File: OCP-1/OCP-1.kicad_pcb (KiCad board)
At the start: 2 copper layers, 15 parts, among them X1 Клеммник_х2

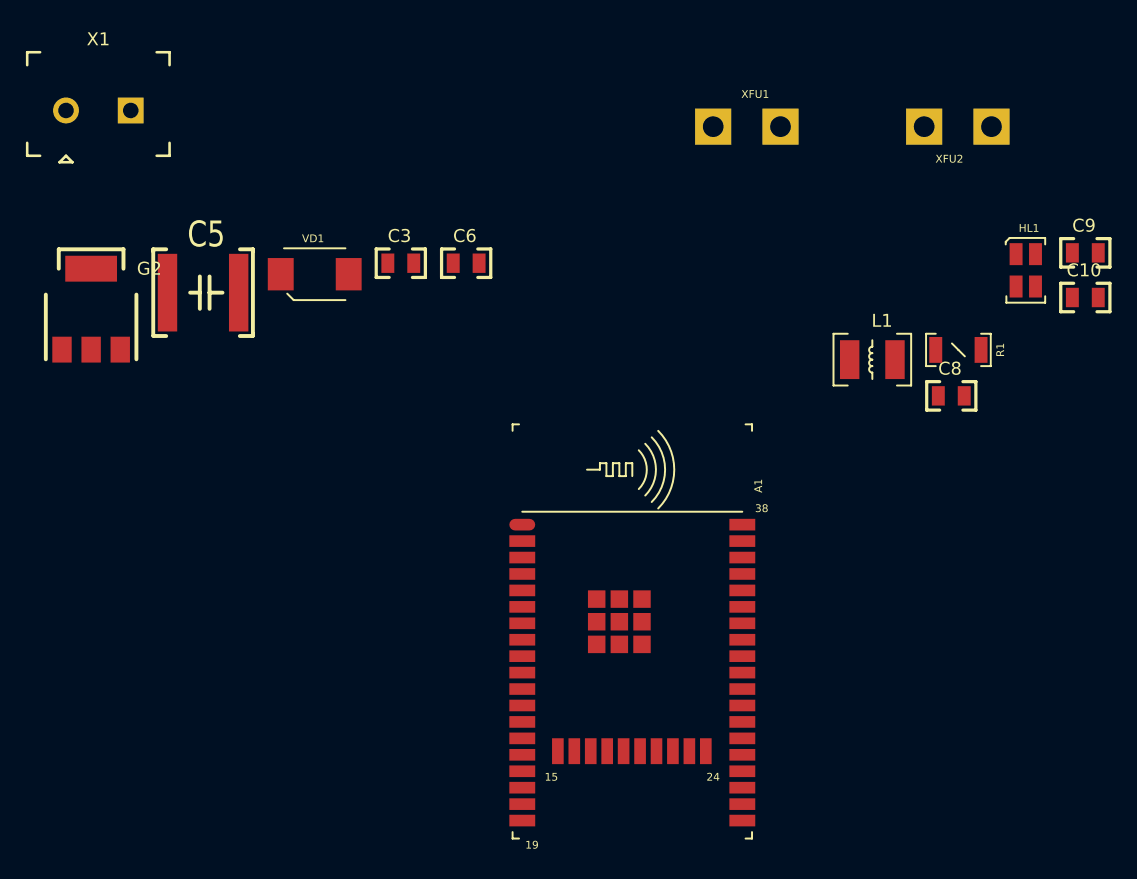
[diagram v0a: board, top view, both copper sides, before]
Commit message: теперь это альтиметр со звуковым оповещением
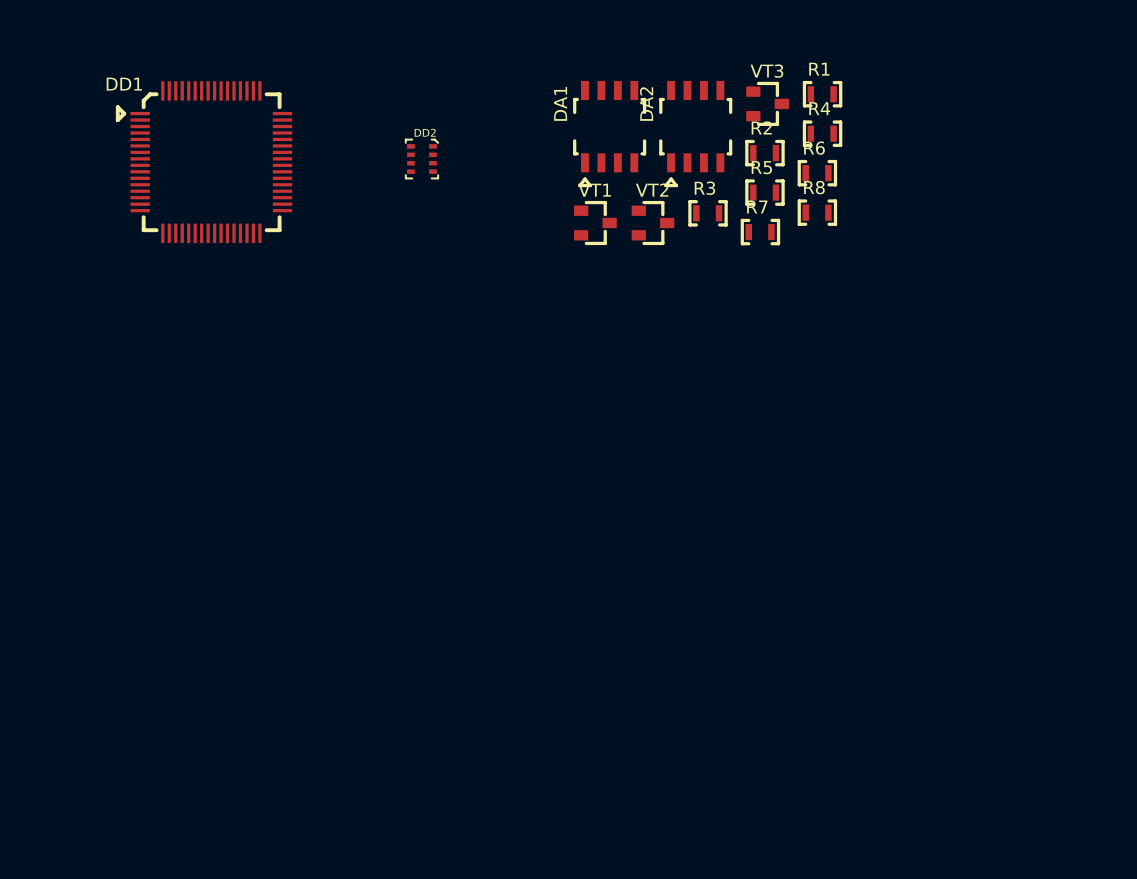
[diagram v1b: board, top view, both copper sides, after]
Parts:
- removed A1: модуль_esp32_wrover_OR_wroom32_SMD, N_A:ESP32_WROVER_or_WROOM32_pnp
- removed C10, C3, C6, C8, C9: Конденсатор_керамический, N_RLC:Конденсатор_SMD_0805
- removed C5: Конденсатор_керамический, N_RLC:Конденсатор_SMD_2220
- removed G2: стабилизатор_нерегулируемый_LM1117S33, N_VD_HL:Транзистор_NPN_SOT223
- removed HL1: Светодиод_сдвоенный_KPB-3025SURKCGKC, N_VD_HL:Светодиод_SMD_m3025
- removed L1: Чип-индуктивность, N_RLC:Чип-индуктивность_SMD_1210
- removed VD1: Диод_шоттки_SK16, N_VD_HL:Диод_SMB_pnp
- removed X1: Клеммник_х2, N_X:Клеммник_х2_шаг5
- removed XFU1, XFU2: Держатель_предохранителя_KLS5-266, N_X:Держатель_5х20
- added DA1: ОУ_LMx58, N_DD:SO-8, F.Cu at (167.0, 67.5)
- added DA2: ОУ_LMx58, N_DD:SO-8, F.Cu at (173.7, 67.5)
- added DD1: 1986ВЕ92QL, N_DD:Микросхема_1986ВЕ92QL, F.Cu at (125.0, 62.5)
- added DD2: BMP280, N_DD:BMP280, F.Cu at (152.5, 70.0)
- added R2: Резистор_0,065Вт, N_RLC:Резистор_SMD_0603_0,065_Вт, F.Cu at (179.0, 69.5)
- added R3: Резистор_0,065Вт, N_RLC:Резистор_SMD_0603_0,065_Вт, F.Cu at (174.6, 74.2)
- added R4: Резистор_0,065Вт, N_RLC:Резистор_SMD_0603_0,065_Вт, F.Cu at (183.4, 68.0)
- added R5: Резистор_0,065Вт, N_RLC:Резистор_SMD_0603_0,065_Вт, F.Cu at (179.0, 72.6)
- added R6: Резистор_0,065Вт, N_RLC:Резистор_SMD_0603_0,065_Вт, F.Cu at (183.0, 71.1)
- added R7: Резистор_0,065Вт, N_RLC:Резистор_SMD_0603_0,065_Вт, F.Cu at (178.6, 75.6)
- added R8: Резистор_0,065Вт, N_RLC:Резистор_SMD_0603_0,065_Вт, F.Cu at (183.0, 74.1)
- added VT1: Транзистор_полевой_P-канал(IRLML2246TRPBF), N_VD_HL:Транзистор_IRLML6344TR_SOT-23, F.Cu at (165.9, 74.9)
- added VT2: Транзистор_полевой_P-канал(IRLML2246TRPBF), N_VD_HL:Транзистор_IRLML6344TR_SOT-23, F.Cu at (170.3, 74.9)
- added VT3: Транзистор_полевой_N-IRLML6344TR, N_VD_HL:Транзистор_IRLML6344TR_SOT-23, F.Cu at (179.2, 65.7)
- R1: value Резистор_0,25Вт -> Резистор_0,065Вт; footprint N_RLC:Резистор_SMD_1206-0,25_Вт_pnp -> N_RLC:Резистор_SMD_0603_0,065_Вт
- moved R1 22.4 mm to (183.4, 65.0)
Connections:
- R1 pad 2: Net-(G1-Pad1) -> /GND

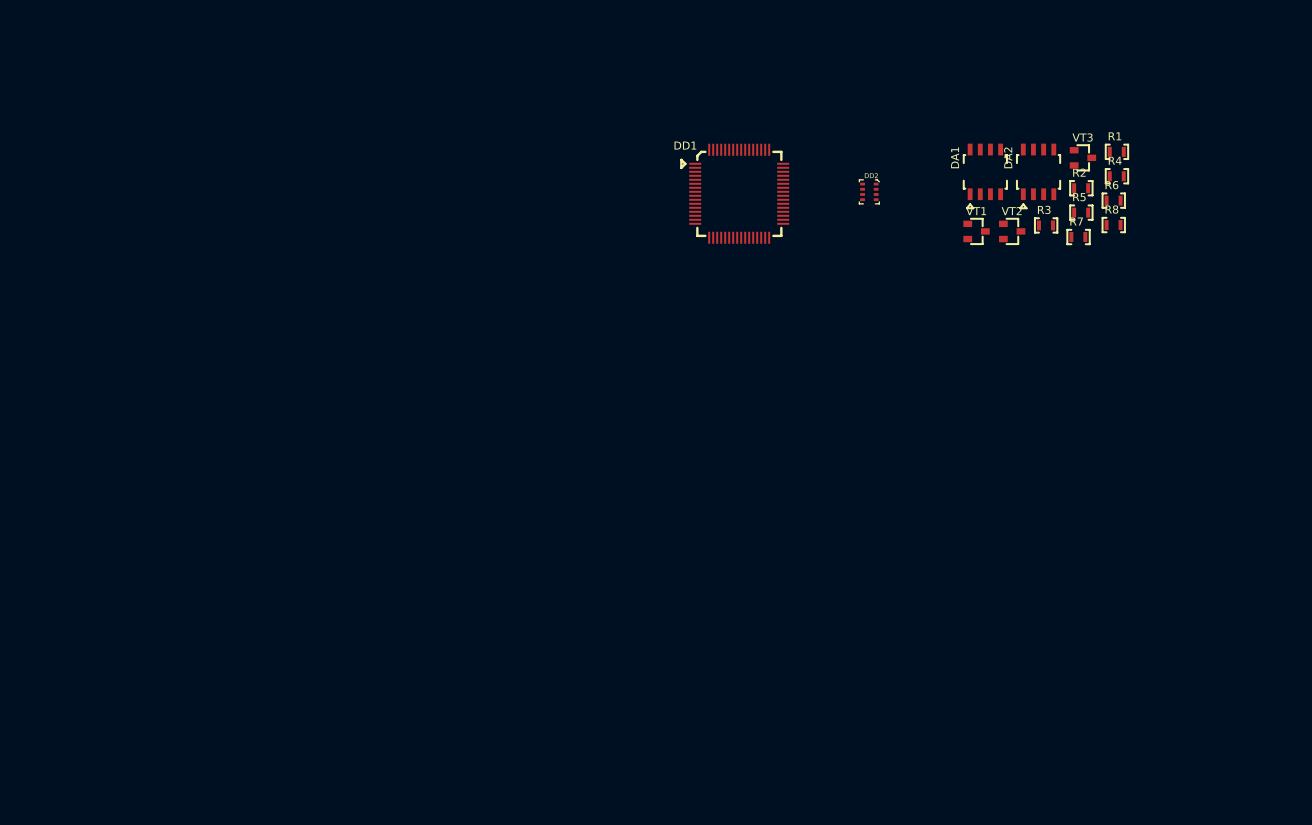
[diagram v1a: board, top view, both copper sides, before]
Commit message: схема заряда аккумулятора и требования к питанию периферии
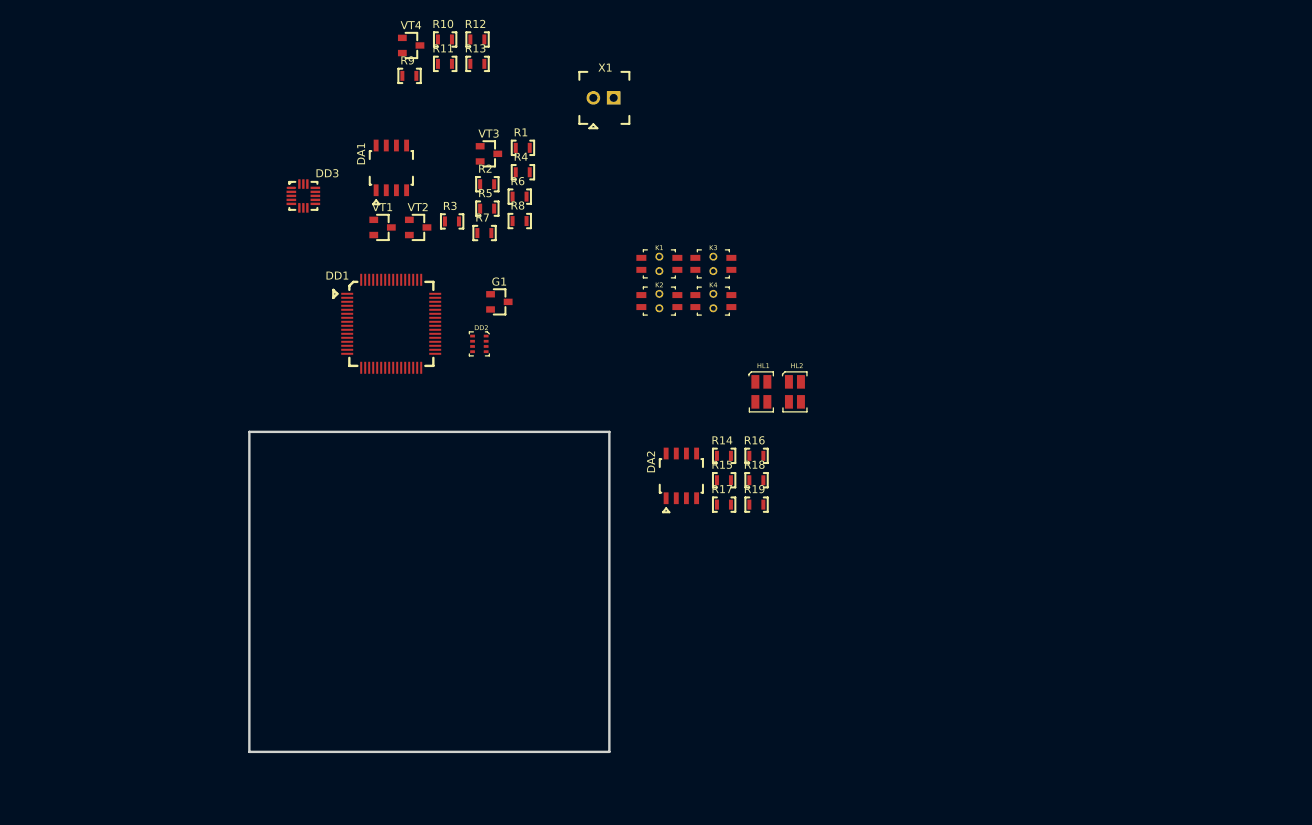
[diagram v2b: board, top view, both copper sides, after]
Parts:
- added DD3: LIS3DH, N_DD:акселерометр_LIS3DH, F.Cu at (81.8, 70.5)
- added G1: ИОП_LM4040BIM3-2.5_NOPB, N_VD_HL:Транзистор_IRLML6344TR_SOT-23, F.Cu at (106.2, 83.8)
- added HL1: Светодиод_сдвоенный_KPB-3025SURKCGKC, N_VD_HL:Светодиод_SMD_m3025, F.Cu at (138.2, 93.8)
- added HL2: Светодиод_сдвоенный_KPB-3025SURKCGKC, N_VD_HL:Светодиод_SMD_m3025, F.Cu at (142.4, 93.8)
- added K1: Кнопка_KLS7-TS5401-1.35-250-T, N_X:Кнопка_KLS7-TS5401, F.Cu at (124.0, 79.8)
- added K2: Кнопка_KLS7-TS5401-1.35-250-T, N_X:Кнопка_KLS7-TS5401, F.Cu at (124.0, 84.4)
- added K3: Кнопка_KLS7-TS5401-1.35-250-T, N_X:Кнопка_KLS7-TS5401, F.Cu at (130.8, 79.8)
- added K4: Кнопка_KLS7-TS5401-1.35-250-T, N_X:Кнопка_KLS7-TS5401, F.Cu at (130.8, 84.4)
- added R10: Резистор_0,065Вт, N_RLC:Резистор_SMD_0603_0,065_Вт, F.Cu at (99.5, 51.0)
- added R11: Резистор_0,065Вт, N_RLC:Резистор_SMD_0603_0,065_Вт, F.Cu at (99.5, 54.0)
- added R12: Резистор_0,065Вт, N_RLC:Резистор_SMD_0603_0,065_Вт, F.Cu at (103.5, 51.0)
- added R13: Резистор_0,065Вт, N_RLC:Резистор_SMD_0603_0,065_Вт, F.Cu at (103.5, 54.0)
- added R14: Резистор_0,065Вт, N_RLC:Резистор_SMD_0603_0,065_Вт, F.Cu at (134.3, 103.0)
- added R15: Резистор_0,065Вт, N_RLC:Резистор_SMD_0603_0,065_Вт, F.Cu at (134.3, 106.0)
- added R16: Резистор_0,065Вт, N_RLC:Резистор_SMD_0603_0,065_Вт, F.Cu at (138.4, 103.0)
- added R17: Резистор_0,065Вт, N_RLC:Резистор_SMD_0603_0,065_Вт, F.Cu at (134.3, 109.1)
- added R18: Резистор_0,065Вт, N_RLC:Резистор_SMD_0603_0,065_Вт, F.Cu at (138.4, 106.0)
- added R19: Резистор_0,065Вт, N_RLC:Резистор_SMD_0603_0,065_Вт, F.Cu at (138.4, 109.1)
- added R9: Резистор_0,065Вт, N_RLC:Резистор_SMD_0603_0,065_Вт, F.Cu at (95.0, 55.5)
- added VT4: Транзистор_полевой_P-канал(IRLML2246TRPBF), N_VD_HL:Транзистор_IRLML6344TR_SOT-23, F.Cu at (95.2, 51.7)
- added X1: Клеммник_х2, N_X:Клеммник_х2_шаг2.54, F.Cu at (118.0, 58.2)
- moved R1 74.3 mm to (109.2, 64.5)
- moved R4 74.3 mm to (109.2, 67.5)
- moved DA1 74.3 mm to (92.8, 67.0)
- moved R2 74.3 mm to (104.7, 69.0)
- moved R5 74.3 mm to (104.7, 72.1)
- moved R6 74.3 mm to (108.8, 70.6)
- moved R7 74.3 mm to (104.4, 75.1)
- moved R8 74.3 mm to (108.8, 73.6)
- moved VT1 74.3 mm to (91.7, 74.4)
- moved VT2 74.3 mm to (96.1, 74.4)
- moved R3 74.3 mm to (100.3, 73.7)
- moved VT3 74.3 mm to (105.0, 65.2)
- moved DA2 58.6 mm to (129.0, 105.5)
- moved DD2 52.3 mm to (103.8, 89.0)
- moved DD1 46.4 mm to (81.5, 78.8)
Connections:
- net Net-(R5-Pad1) renamed /CUR.SENS
- DA1 pad 2: (no net) -> /2V5.REF
- DA1 pad 3: /4V2.OUT -> /2V5.OUT
- DA1 pad 5: (no net) -> /DIFF.AMP
- DA1 pad 6: (no net) -> /1V5.REF
- DA1 pad 7: (no net) -> /CUR.DIRECT
- DA2 pad 1: (no net) -> /DIFF.AMP
- DA2 pad 2: (no net) -> Net-(DA2-Pad2)
- DA2 pad 3: (no net) -> Net-(DA2-Pad3)
- DA2 pad 4: (no net) -> /GND
- DA2 pad 5: (no net) -> /CUR.OUT
- DA2 pad 6: (no net) -> /REP.SENS-
- DA2 pad 7: (no net) -> /REP.SENS-
- DA2 pad 8: (no net) -> /5V.LINE
- R3 pad 1: /5V.LINE -> /CUR.OUT
- R5 pad 2: Net-(R5-Pad2) -> /CUR.OUT
- R6 pad 2: Net-(R5-Pad2) -> /CUR.OUT
- R7 pad 2: Net-(R5-Pad2) -> /CUR.OUT
- R8 pad 2: Net-(R5-Pad2) -> /CUR.OUT
- VT2 pad 2: /5V.LINE -> /CUR.OUT
- VT2 pad 3: /4V2.OUT -> /4V1.OUT
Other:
- board outline added: 45 x 40 mm

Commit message: схема питания МК и датчиков
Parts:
- added C1: Конденсатор_керамический, N_RLC:Конденсатор_SMD_IEC_0805, F.Cu at (57.8, 66.8)
- added C2: Конденсатор_керамический, N_RLC:Конденсатор_SMD_IEC_0805, F.Cu at (64.4, 57.5)
- added C3: Конденсатор_керамический, N_RLC:Конденсатор_SMD_IEC_0805, F.Cu at (64.4, 60.7)
- added C4: Конденсатор_керамический, N_RLC:Конденсатор_SMD_IEC_0805, F.Cu at (65.0, 63.9)
- added C5: Конденсатор_керамический, N_RLC:Конденсатор_SMD_IEC_0805, F.Cu at (71.7, 57.5)
- added C6: Конденсатор_керамический, N_RLC:Конденсатор_SMD_IEC_0805, F.Cu at (71.7, 60.7)
- added C7: Конденсатор_керамический, N_RLC:Конденсатор_SMD_IEC_0805, F.Cu at (65.0, 67.0)
- added DA3: ОУ_LMx58, N_DD:SO-8, F.Cu at (58.4, 60.0)
- added G3: LDO_TPS76325DBVR, N_G:Преобразователь_LM2703_SOT-23-5, F.Cu at (74.0, 89.2)
- added G4: LDO_TPS76318DBVT, N_G:Преобразователь_LM2703_SOT-23-5, F.Cu at (78.5, 89.2)
- added R20: Резистор_0,065Вт, N_RLC:Резистор_SMD_0603_0,065_Вт, F.Cu at (57.0, 69.8)
- added R21: Резистор_0,065Вт, N_RLC:Резистор_SMD_0603_0,065_Вт, F.Cu at (78.2, 57.5)
- added R22: Резистор_0,065Вт, N_RLC:Резистор_SMD_0603_0,065_Вт, F.Cu at (78.2, 60.5)
- added R23: Резистор_0,065Вт, N_RLC:Резистор_SMD_0603_0,065_Вт, F.Cu at (71.6, 68.3)
- VT3: value Транзистор_полевой_N-IRLML6344TR -> Транзистор_полевой_P-канал(IRLML2246TRPBF)
- moved VT3 33.2 mm to (71.8, 64.5)
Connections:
- net /2V5.OUT renamed /2V5.FB1
- DD1 pad 1: (no net) -> Net-(DD1-Pad1)
- DD1 pad 10: (no net) -> Net-(DD1-Pad10)
- DD1 pad 11: (no net) -> Net-(DD1-Pad11)
- DD1 pad 12: (no net) -> Net-(DD1-Pad12)
- DD1 pad 13: (no net) -> Net-(DD1-Pad13)
- DD1 pad 14: (no net) -> Net-(DD1-Pad14)
- DD1 pad 15: (no net) -> Net-(DD1-Pad15)
- DD1 pad 16: (no net) -> Net-(DD1-Pad16)
- DD1 pad 17: (no net) -> Net-(DD1-Pad17)
- DD1 pad 18: (no net) -> Net-(DD1-Pad18)
- DD1 pad 19: (no net) -> Net-(DD1-Pad19)
- DD1 pad 2: (no net) -> Net-(DD1-Pad2)
- DD1 pad 20: (no net) -> Net-(DD1-Pad20)
- DD1 pad 21: (no net) -> Net-(DD1-Pad21)
- DD1 pad 22: (no net) -> Net-(DD1-Pad22)
- DD1 pad 23: (no net) -> Net-(DD1-Pad23)
- DD1 pad 24: (no net) -> Net-(DD1-Pad24)
- DD1 pad 25: (no net) -> Net-(DD1-Pad25)
- DD1 pad 26: (no net) -> Net-(DD1-Pad26)
- DD1 pad 27: (no net) -> Net-(DD1-Pad27)
- DD1 pad 28: (no net) -> Net-(DD1-Pad28)
- DD1 pad 29: (no net) -> Net-(DD1-Pad29)
- DD1 pad 3: (no net) -> Net-(DD1-Pad3)
- DD1 pad 30: (no net) -> Net-(DD1-Pad30)
- DD1 pad 31: (no net) -> Net-(DD1-Pad31)
- DD1 pad 32: (no net) -> Net-(DD1-Pad32)
- DD1 pad 33: (no net) -> Net-(DD1-Pad33)
- DD1 pad 34: (no net) -> Net-(DD1-Pad34)
- DD1 pad 35: (no net) -> Net-(DD1-Pad35)
- DD1 pad 36: (no net) -> Net-(DD1-Pad36)
- DD1 pad 37: (no net) -> Net-(DD1-Pad37)
- DD1 pad 38: (no net) -> Net-(DD1-Pad38)
- DD1 pad 39: (no net) -> Net-(DD1-Pad39)
- DD1 pad 4: (no net) -> Net-(DD1-Pad4)
- DD1 pad 40: (no net) -> Net-(DD1-Pad40)
- DD1 pad 41: (no net) -> Net-(DD1-Pad41)
- DD1 pad 42: (no net) -> Net-(DD1-Pad42)
- DD1 pad 43: (no net) -> Net-(DD1-Pad43)
- DD1 pad 44: (no net) -> Net-(DD1-Pad44)
- DD1 pad 45: (no net) -> Net-(DD1-Pad45)
- DD1 pad 46: (no net) -> Net-(DD1-Pad46)
- DD1 pad 47: (no net) -> Net-(DD1-Pad47)
- DD1 pad 48: (no net) -> Net-(DD1-Pad48)
- DD1 pad 49: (no net) -> Net-(DD1-Pad49)
- DD1 pad 5: (no net) -> Net-(DD1-Pad5)
- DD1 pad 50: (no net) -> Net-(DD1-Pad50)
- DD1 pad 51: (no net) -> Net-(DD1-Pad51)
- DD1 pad 52: (no net) -> Net-(DD1-Pad52)
- DD1 pad 53: (no net) -> Net-(DD1-Pad53)
- DD1 pad 54: (no net) -> Net-(DD1-Pad54)
- DD1 pad 55: (no net) -> Net-(DD1-Pad55)
- DD1 pad 56: (no net) -> Net-(DD1-Pad56)
- DD1 pad 57: (no net) -> Net-(DD1-Pad57)
- DD1 pad 58: (no net) -> Net-(DD1-Pad58)
- DD1 pad 59: (no net) -> Net-(DD1-Pad59)
- DD1 pad 6: (no net) -> Net-(DD1-Pad6)
- DD1 pad 60: (no net) -> Net-(DD1-Pad60)
- DD1 pad 61: (no net) -> Net-(DD1-Pad61)
- DD1 pad 62: (no net) -> Net-(DD1-Pad62)
- DD1 pad 63: (no net) -> Net-(DD1-Pad63)
- DD1 pad 64: (no net) -> Net-(DD1-Pad64)
- DD1 pad 7: (no net) -> Net-(DD1-Pad7)
- DD1 pad 8: (no net) -> Net-(DD1-Pad8)
- DD1 pad 9: (no net) -> Net-(DD1-Pad9)
- DD2 pad 1: (no net) -> Net-(DD2-Pad1)
- DD2 pad 2: (no net) -> Net-(DD2-Pad2)
- DD2 pad 3: (no net) -> Net-(DD2-Pad3)
- DD2 pad 4: (no net) -> Net-(DD2-Pad4)
- DD2 pad 5: (no net) -> Net-(DD2-Pad5)
- DD2 pad 6: (no net) -> Net-(DD2-Pad6)
- DD2 pad 7: (no net) -> Net-(DD2-Pad7)
- DD2 pad 8: (no net) -> Net-(DD2-Pad8)
- DD3 pad 1: (no net) -> Net-(DD3-Pad1)
- DD3 pad 10: (no net) -> Net-(DD3-Pad10)
- DD3 pad 11: (no net) -> Net-(DD3-Pad11)
- DD3 pad 12: (no net) -> Net-(DD3-Pad12)
- DD3 pad 13: (no net) -> Net-(DD3-Pad13)
- DD3 pad 14: (no net) -> Net-(DD3-Pad14)
- DD3 pad 15: (no net) -> Net-(DD3-Pad15)
- DD3 pad 16: (no net) -> Net-(DD3-Pad16)
- DD3 pad 2: (no net) -> Net-(DD3-Pad2)
- DD3 pad 3: (no net) -> Net-(DD3-Pad3)
- DD3 pad 4: (no net) -> Net-(DD3-Pad4)
- DD3 pad 5: (no net) -> Net-(DD3-Pad5)
- DD3 pad 6: (no net) -> Net-(DD3-Pad6)
- DD3 pad 7: (no net) -> Net-(DD3-Pad7)
- DD3 pad 8: (no net) -> Net-(DD3-Pad8)
- DD3 pad 9: (no net) -> Net-(DD3-Pad9)
- G1 pad 3: (no net) -> Net-(G1-Pad3)
- HL1 pad 1: (no net) -> Net-(HL1-Pad1)
- HL1 pad 2: (no net) -> Net-(HL1-Pad2)
- HL1 pad 3: (no net) -> Net-(HL1-Pad3)
- HL1 pad 4: (no net) -> Net-(HL1-Pad4)
- HL2 pad 1: (no net) -> Net-(HL2-Pad1)
- HL2 pad 2: (no net) -> Net-(HL2-Pad2)
- HL2 pad 3: (no net) -> Net-(HL2-Pad3)
- HL2 pad 4: (no net) -> Net-(HL2-Pad4)
- K1 pad 1: (no net) -> Net-(K1-Pad1)
- K1 pad 2: (no net) -> Net-(K1-Pad2)
- K1 pad 3: (no net) -> Net-(K1-Pad3)
- K1 pad 4: (no net) -> Net-(K1-Pad4)
- K2 pad 1: (no net) -> Net-(K2-Pad1)
- K2 pad 2: (no net) -> Net-(K2-Pad2)
- K2 pad 3: (no net) -> Net-(K2-Pad3)
- K2 pad 4: (no net) -> Net-(K2-Pad4)
- K3 pad 1: (no net) -> Net-(K3-Pad1)
- K3 pad 2: (no net) -> Net-(K3-Pad2)
- K3 pad 3: (no net) -> Net-(K3-Pad3)
- K3 pad 4: (no net) -> Net-(K3-Pad4)
- K4 pad 1: (no net) -> Net-(K4-Pad1)
- K4 pad 2: (no net) -> Net-(K4-Pad2)
- K4 pad 3: (no net) -> Net-(K4-Pad3)
- K4 pad 4: (no net) -> Net-(K4-Pad4)
- VT1 pad 3: (no net) -> /5V.IN
- VT3 pad 1: (no net) -> Net-(R20-Pad2)
- VT3 pad 2: (no net) -> /4V1.OUT
- VT3 pad 3: (no net) -> /3V1
